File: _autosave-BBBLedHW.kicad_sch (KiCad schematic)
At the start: 40 parts, among them J3 Barrel_Jack_Switch, Q1 2N7002, U1 STM32WB55CEUx, U2 TPS7A2033DBV, U3 SN74LVC1T45DBV, U4 ADP2303ARDZ-5.0, X1 32MHz, X2 32kHz768

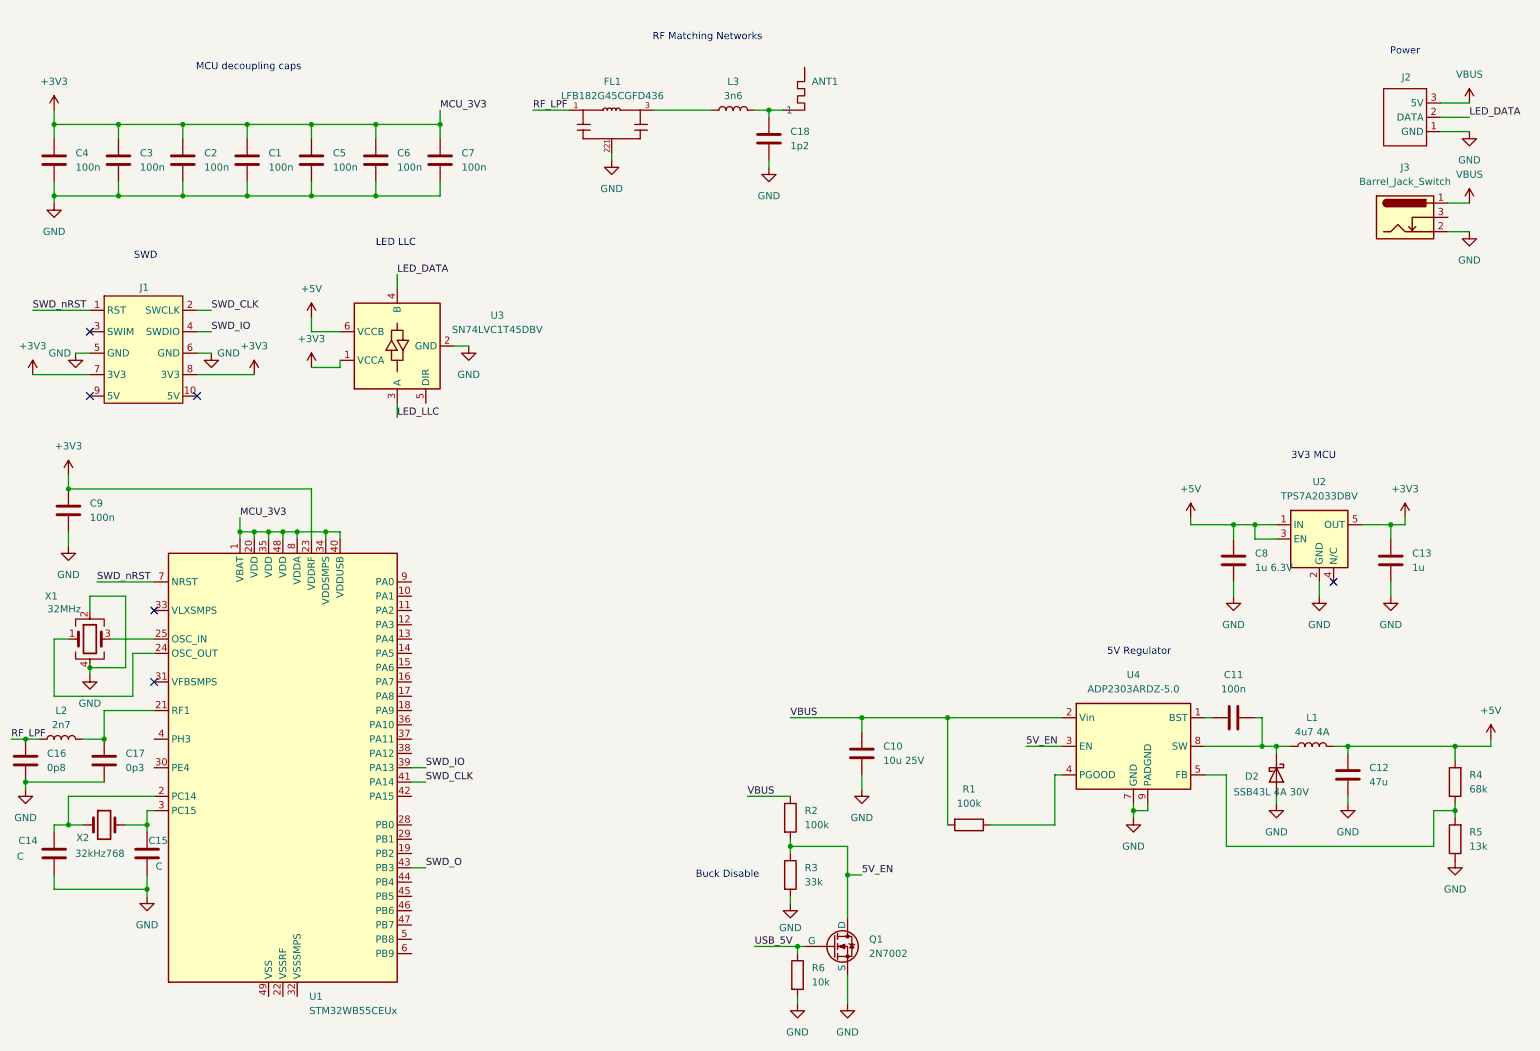
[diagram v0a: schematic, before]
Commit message: Added 5V regulator disable circuit and DC+USB power connectors
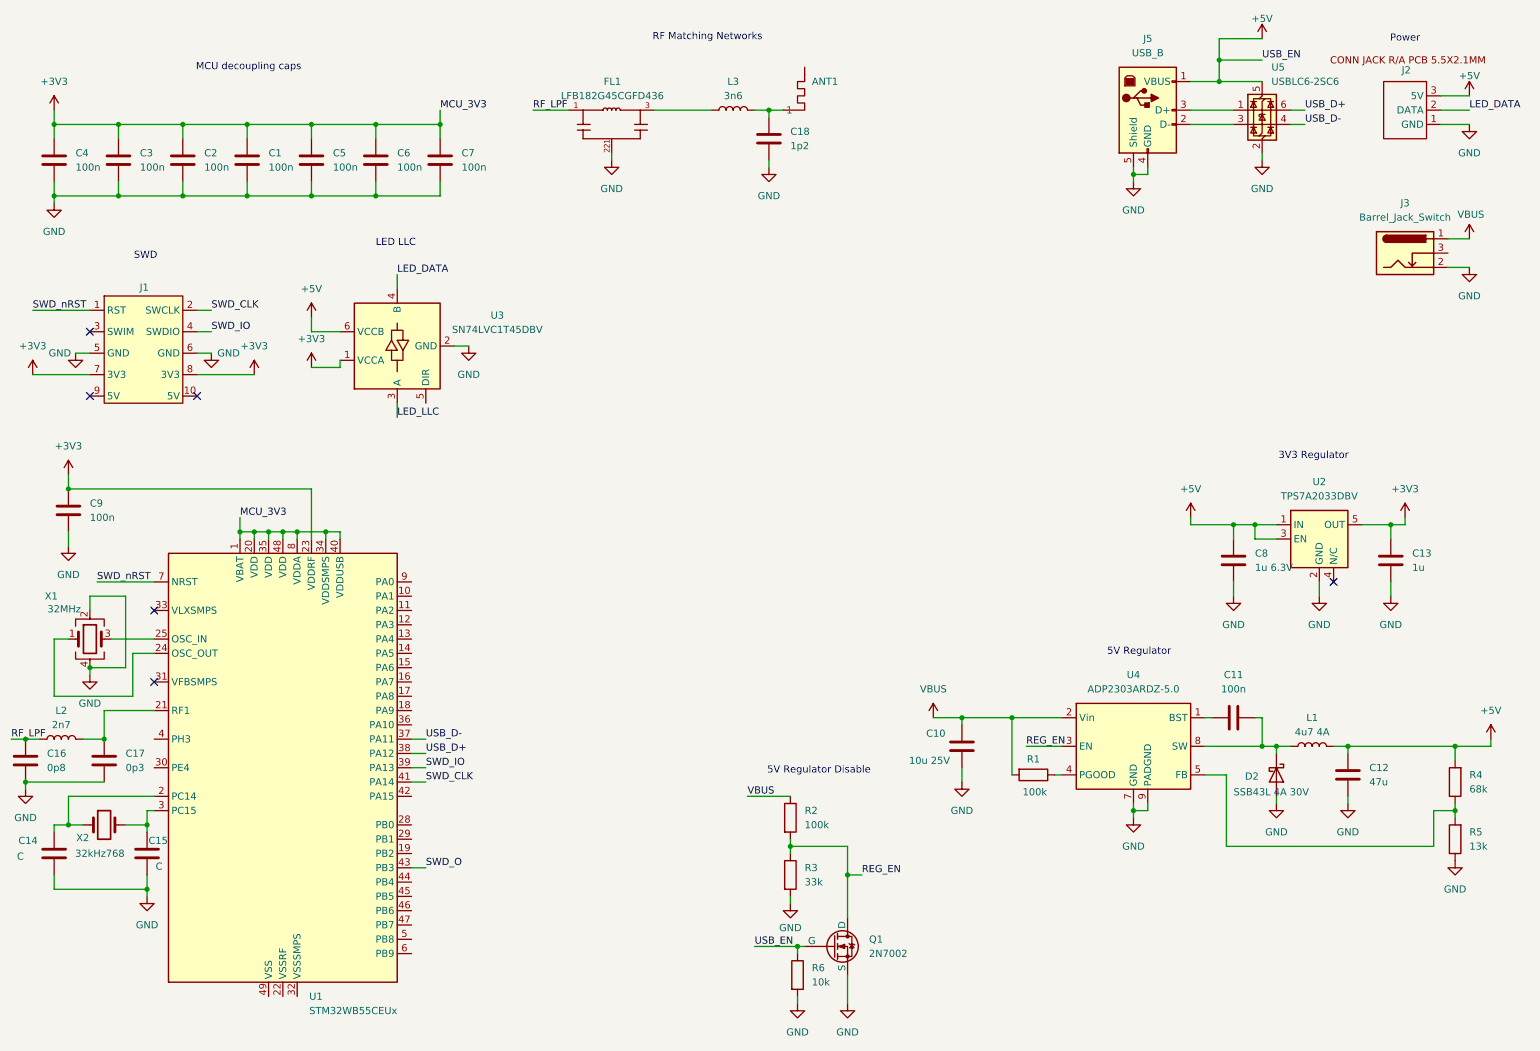
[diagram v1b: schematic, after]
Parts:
- added J5: USB_B, symbol Connector:USB_B
- added U5: USBLC6-2SC6, Package_TO_SOT_SMD:SOT-23-6, symbol Power_Protection:USBLC6-2SC6
- J2: value ~ -> CONN JACK R/A PCB 5.5X2.1MM
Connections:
- net USB_5V is gone; now on net +5V: Q1.2 (G), R6.1
- net +5V: now also J2.3 (5V), J5.1 (VBUS), U5.5 (VBUS)
- net GND: now also J5.4 (GND), J5.5 (Shield), U5.2 (GND)
- net VBUS: no longer J2.3 (5V)
- net USB_D-: now reaches U1.37 (PA11)
- net USB_D-: now also U5.4 (I/O2)
- net USB_D+: now reaches U1.38 (PA12)
- net USB_D+: now also U5.6 (I/O1)
- net 5V_EN renamed REG_EN
- new net: J5.3 (D+), U5.1 (I/O1)
- new net: J5.2 (D-), U5.3 (I/O2)
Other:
- note added: "3V3 Regulator"
- note added: "5V Regulator Disable"
- note removed: "3V3 MCU"
- note removed: "Buck Disable"
- moved on the sheet: C10, J3, R1
